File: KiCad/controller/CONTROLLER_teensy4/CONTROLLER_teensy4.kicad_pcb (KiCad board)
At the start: 4 copper layers, 19 x 36.5 mm, 10 parts, among them J5 jack2.5_PJ-210B, U1 Teensy4.0

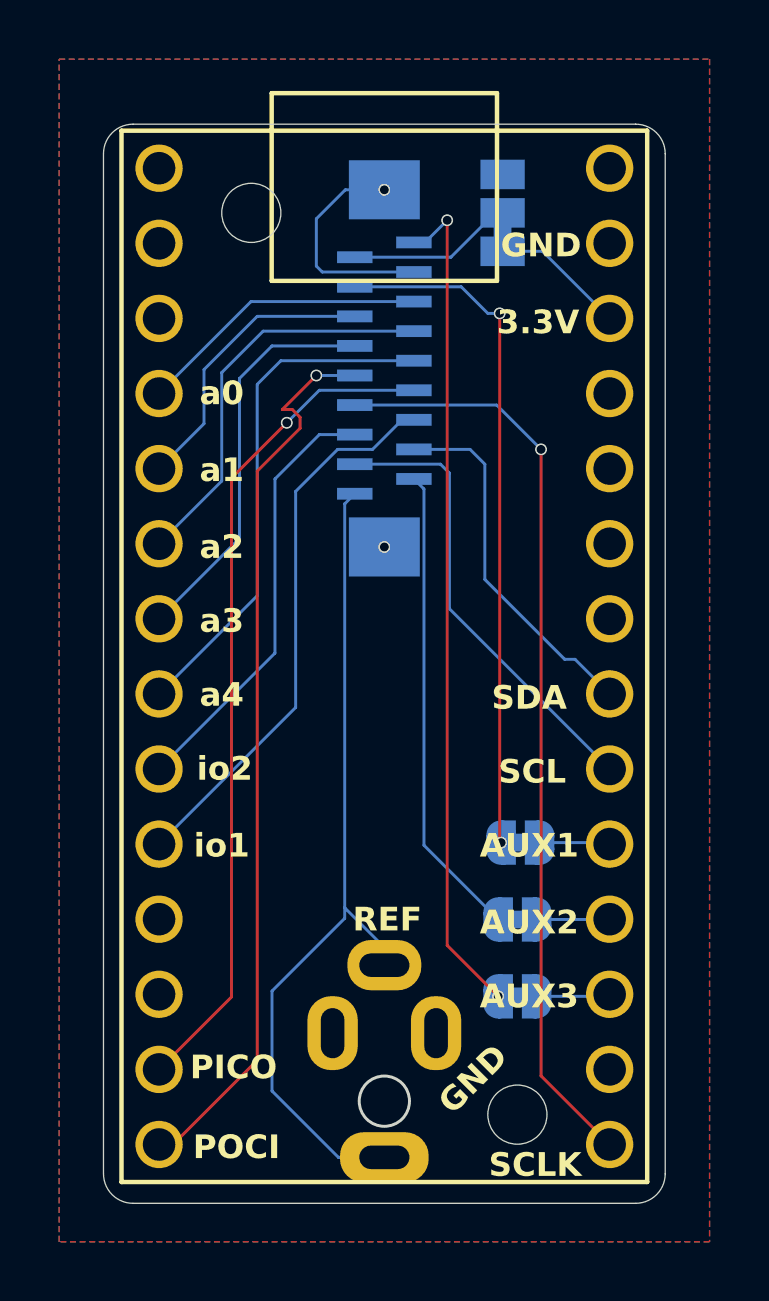
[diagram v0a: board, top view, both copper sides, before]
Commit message: major update: fixed inversion of i2c lines + added pull up resistors + rotated 180deg fpc conector
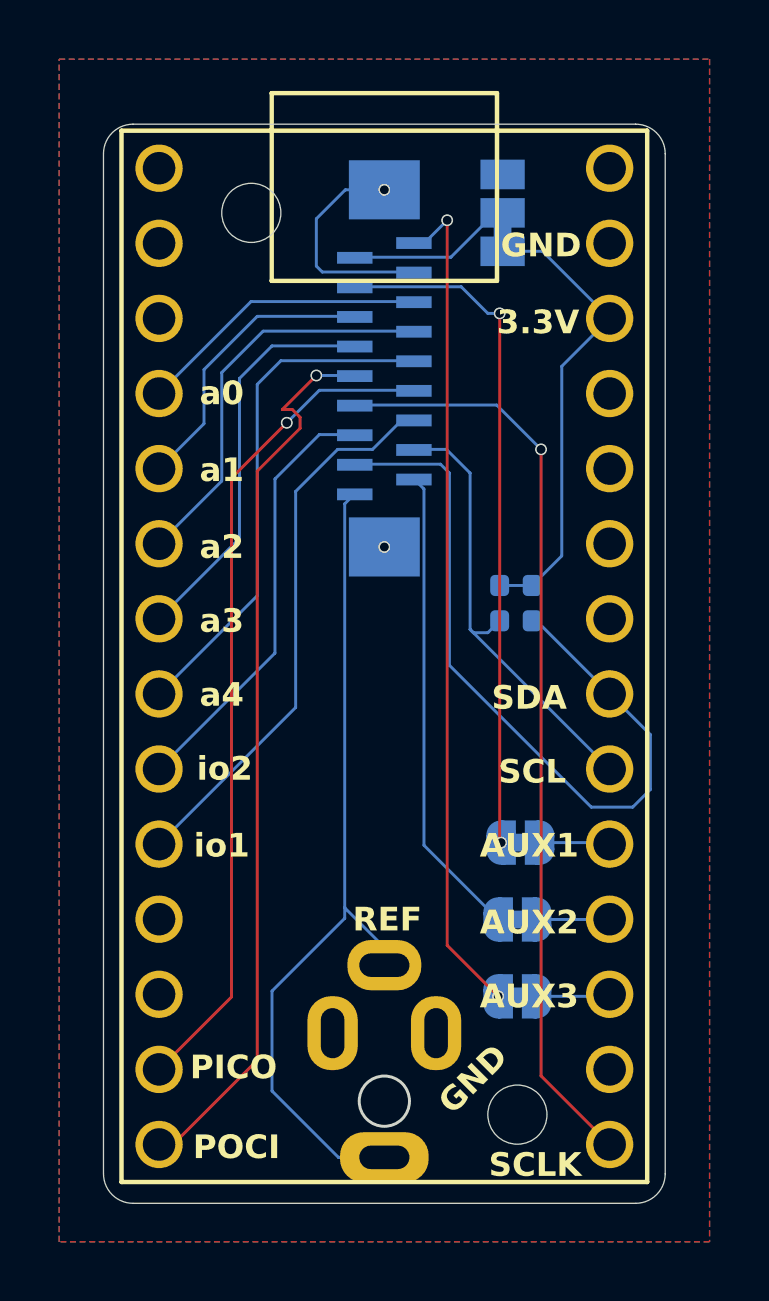
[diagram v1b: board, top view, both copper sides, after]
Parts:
- removed FPC2: FPC-05F-18PH20, 00_lcsc:FPC-SMD_18P-P0.50_X05C2018TZ
- added FPC1: FPC-05F-18PH20, 00_lcsc:FPC-SMD_18P-P0.50_X05C2018TZ, B.Cu at (100.0, 74.3)
- added R1: 2k, Resistor_SMD:R_0402_1005Metric_Pad0.72x0.64mm_HandSolder, B.Cu at (105.0, 82.2)
- added R2: 2k, Resistor_SMD:R_0402_1005Metric_Pad0.72x0.64mm_HandSolder, B.Cu at (103.9, 82.2)
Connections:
- U1 pad 25: /i2C_SCL -> /I2C_SDA
- U1 pad 26: /I2C_SDA -> /i2C_SCL
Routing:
- net 3V3_TEENSY: track 4.56 -> 15.8 mm
- net /i2C_SCL: track 15.6 -> 26.3 mm
- net /I2C_SDA: track 12.3 -> 15.4 mm

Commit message: minor fix on teensy shield
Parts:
- removed JP4: SolderJumper_3_Bridged12, Jumper:SolderJumper-3_P1.3mm_Bridged12_Pad1.0x1.5mm
- added J2: Conn_01x02_Pin, Connector_PinHeader_1.27mm:PinHeader_1x02_P1.27mm_Vertical, F.Cu at (104.1, 67.4)
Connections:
- R1 pad 1: 3V3_TEENSY -> +3.3V
- R2 pad 1: 3V3_TEENSY -> +3.3V
- U1 pad 31: 3V3_TEENSY -> +3.3V
- U1 pad 33: unconnected-(U1-VIN-Pad33) -> VSYS
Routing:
- net 3V3_TEENSY: track 15.8 -> 0.00 mm
- net +3.3V: track 5.62 -> 20.7 mm
- net GND: track 7.69 -> 12.1 mm
- net VSYS: track 0.00 -> 3.60 mm
